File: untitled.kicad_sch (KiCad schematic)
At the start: 24 parts, among them J10_GPIO1 Conn_01x02, J11_SPI1 Conn_01x03, J2 Conn_01x04_Pin, J3 Conn_01x04_Pin, J4 Conn_01x02_Pin, J5 Conn_01x04_Pin, J6 Conn_01x04_Pin, J7 Conn_01x02_Pin, J9_GPIO1 Conn_01x02, J9_GPIO2 Conn_01x02

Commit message: Version 1.1 - reworked all smd's to 0603
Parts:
- R26, R31, R32, R33, R34: footprint Resistor_SMD:R_0201_0603Metric_Pad0.64x0.40mm_HandSolder -> Resistor_SMD:R_0603_1608Metric_Pad0.98x0.95mm_HandSolder
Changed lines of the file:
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@@
       (effects (font (size 1.27 1.27)) (justify left))
     )
-    (property "Footprint" "Resistor_SMD:R_0201_0603Metric_Pad0.64x0.40mm_HandSolder" (at 239.522 132.08 90)
+    (property "Footprint" "Resistor_SMD:R_0603_1608Metric_Pad0.98x0.95mm_HandSolder" (at 239.522 132.08 90)
       (effects (font (size 1.27 1.27)) hide)
     )
@@
       (effects (font (size 1.27 1.27)) (justify left))
     )
-    (property "Footprint" "Resistor_SMD:R_0201_0603Metric_Pad0.64x0.40mm_HandSolder" (at 210.312 69.85 90)
+    (property "Footprint" "Resistor_SMD:R_0603_1608Metric_Pad0.98x0.95mm_HandSolder" (at 210.312 69.85 90)
       (effects (font (size 1.27 1.27)) hide)
     )
@@
       (effects (font (size 1.27 1.27)) (justify left))
     )
-    (property "Footprint" "Resistor_SMD:R_0201_0603Metric_Pad0.64x0.40mm_HandSolder" (at 261.112 74.93 90)
+    (property "Footprint" "Resistor_SMD:R_0603_1608Metric_Pad0.98x0.95mm_HandSolder" (at 261.112 74.93 90)
       (effects (font (size 1.27 1.27)) hide)
     )
@@
       (effects (font (size 1.27 1.27)) (justify left))
     )
-    (property "Footprint" "Resistor_SMD:R_0201_0603Metric_Pad0.64x0.40mm_HandSolder" (at 256.032 74.93 90)
+    (property "Footprint" "Resistor_SMD:R_0603_1608Metric_Pad0.98x0.95mm_HandSolder" (at 256.032 74.93 90)
       (effects (font (size 1.27 1.27)) hide)
     )
@@
       (effects (font (size 1.27 1.27)) (justify left))
     )
-    (property "Footprint" "Resistor_SMD:R_0201_0603Metric_Pad0.64x0.40mm_HandSolder" (at 215.392 69.85 90)
+    (property "Footprint" "Resistor_SMD:R_0603_1608Metric_Pad0.98x0.95mm_HandSolder" (at 215.392 69.85 90)
       (effects (font (size 1.27 1.27)) hide)
     )
@@
       (effects (font (size 1.27 1.27)) (justify left))
     )
-    (property "Footprint" "Resistor_SMD:R_0201_0603Metric_Pad0.64x0.40mm_HandSolder" (at 259.842 132.08 90)
-      (effects (font (size 1.27 1.27)) hide)
-    )
+    (property "Footprint" "Resistor_SMD:R_0603_1608Metric_Pad0.98x0.95mm_HandSolder" (at 259.842 132.08 90)
+      (effects (font (size 1.27 1.27)) hide)
+    )

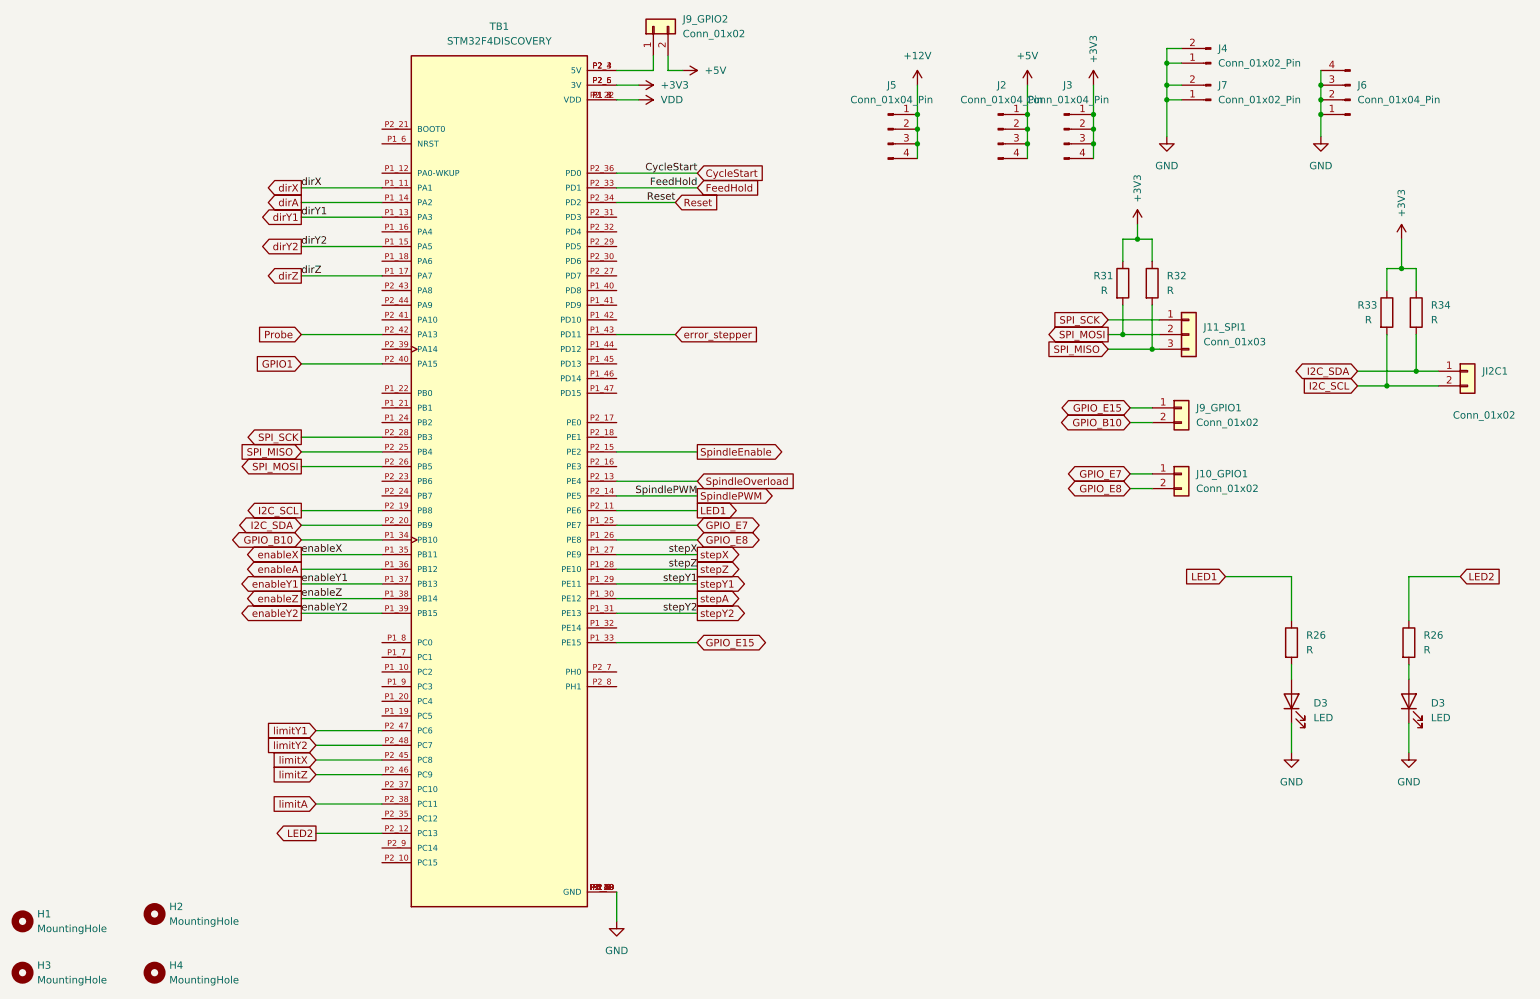
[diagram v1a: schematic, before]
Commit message: Adding Coolant and Mist; some GPIOs added
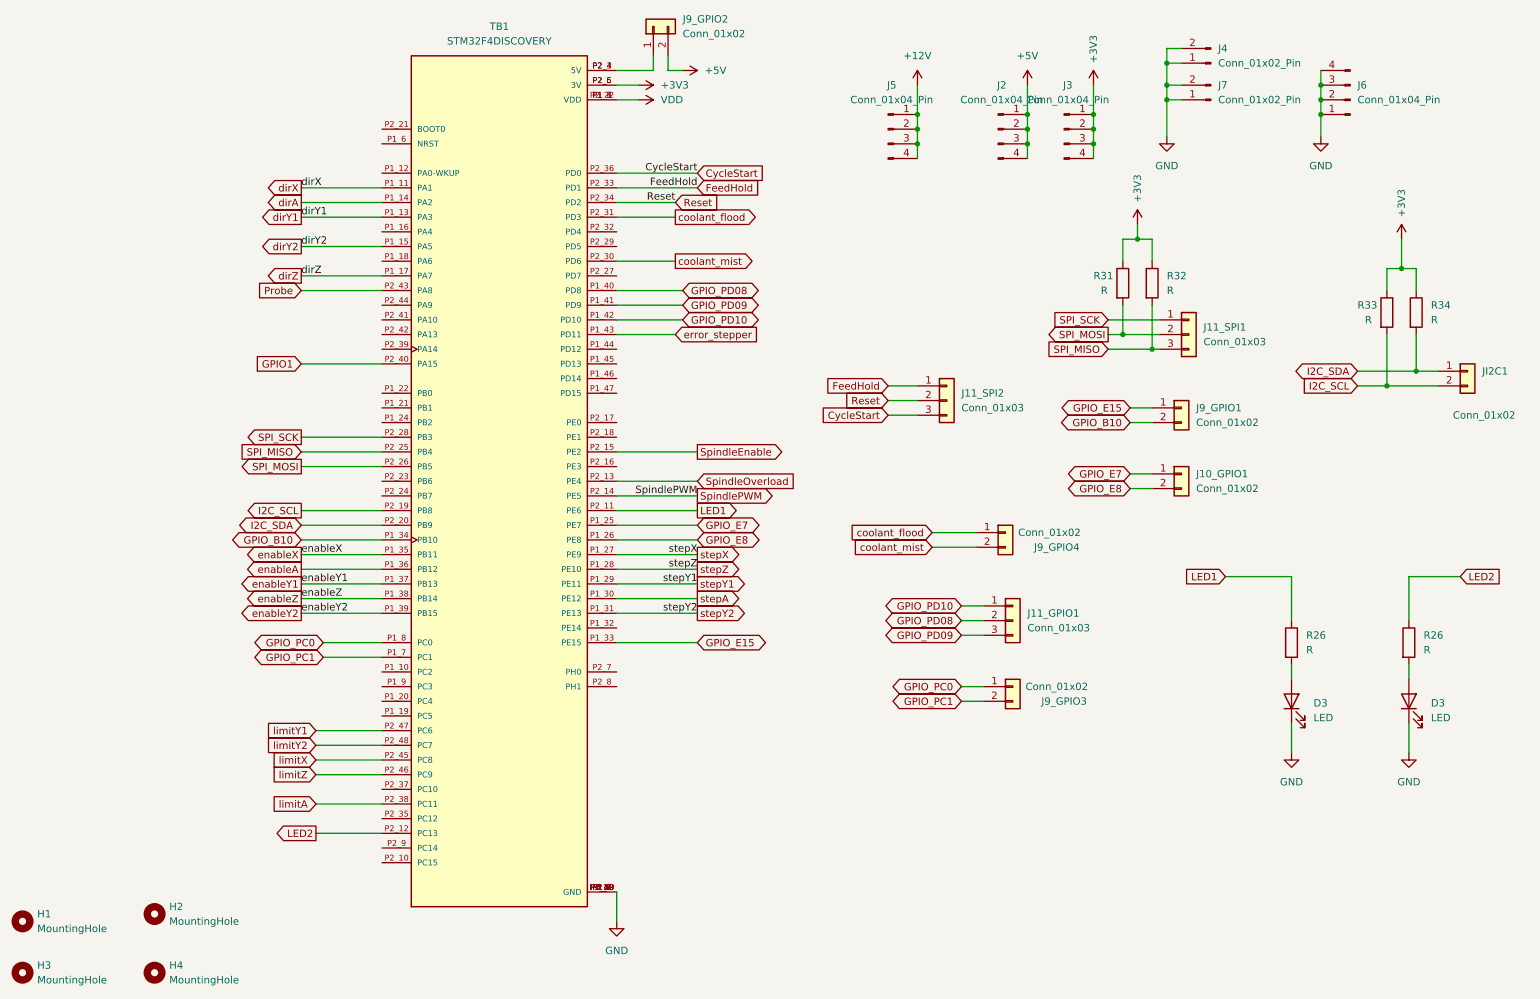
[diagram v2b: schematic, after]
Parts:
- added J11_GPIO1, J11_SPI2: Conn_01x03, Connector_PinHeader_2.54mm:PinHeader_1x03_P2.54mm_Vertical, symbol Connector_Generic:Conn_01x03
- added J9_GPIO3, J9_GPIO4: Conn_01x02, Connector_PinHeader_2.54mm:PinHeader_1x02_P2.54mm_Vertical, symbol Connector_Generic:Conn_01x02
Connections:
- net CycleStart: now also J11_SPI2.3 (Pin_3)
- net FeedHold: now also J11_SPI2.1 (Pin_1)
- net Probe: now also TB1.P2_43 (PA8); no longer TB1.P2_42 (PA13)
- net Reset: now also J11_SPI2.2 (Pin_2)
- net GPIO_PD08: now reaches TB1.P1_40 (PD8)
- net GPIO_PD08: now also J11_GPIO1.2 (Pin_2)
- net GPIO_PD09: now reaches TB1.P1_41 (PD9)
- net GPIO_PD09: now also J11_GPIO1.3 (Pin_3)
- net GPIO_PD10: now reaches TB1.P1_42 (PD10)
- net GPIO_PD10: now also J11_GPIO1.1 (Pin_1)
- net GPIO_PC1: now reaches TB1.P1_7 (PC1)
- net GPIO_PC1: now also J9_GPIO3.2 (Pin_2)
- net GPIO_PC0: now reaches TB1.P1_8 (PC0)
- net GPIO_PC0: now also J9_GPIO3.1 (Pin_1)
- net coolant_mist: now reaches TB1.P2_30 (PD6)
- net coolant_mist: now also J9_GPIO4.2 (Pin_2)
- net coolant_flood: now reaches TB1.P2_31 (PD3)
- net coolant_flood: now also J9_GPIO4.1 (Pin_1)

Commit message: Updating for version 1.1
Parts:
- R26: value R -> 510
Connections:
- net dirA: now also TB1.P1_17 (PA7); no longer TB1.P1_14 (PA2)
- net dirY2: now also TB1.P1_12 (PA0-WKUP); no longer TB1.P1_15 (PA5)
- net dirZ: now also TB1.P1_14 (PA2); no longer TB1.P1_17 (PA7)

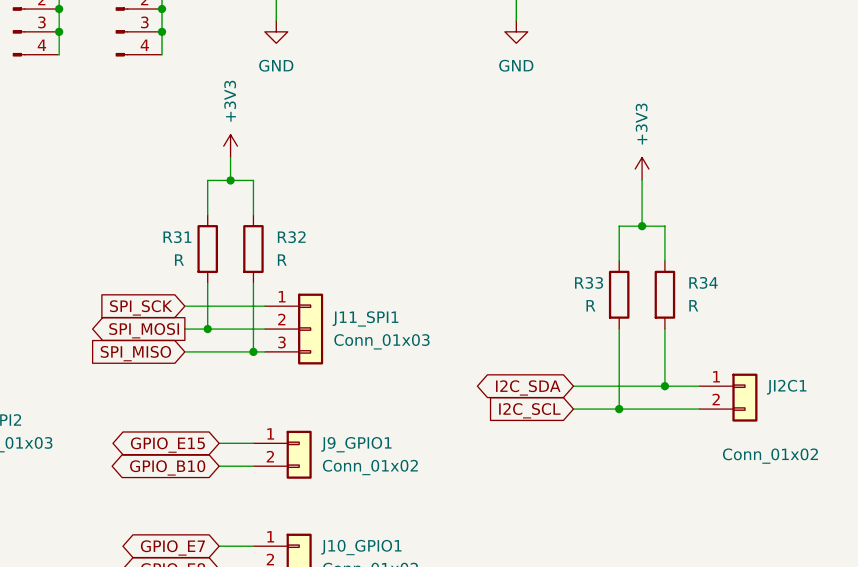
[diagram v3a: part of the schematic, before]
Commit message: Mainly value updates
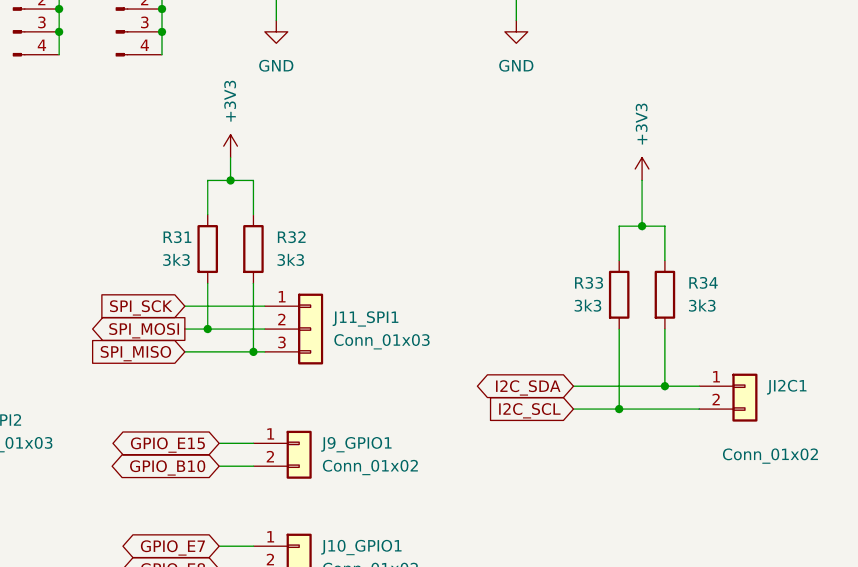
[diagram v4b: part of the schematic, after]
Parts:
- R31, R32, R33, R34: value R -> 3k3
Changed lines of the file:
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@@
       (effects (font (size 1.27 1.27)) (justify left))
     )
-    (property "Value" "R" (at 208.28 71.12 0)
+    (property "Value" "3k3" (at 207.01 71.12 0)
       (effects (font (size 1.27 1.27)) (justify left))
     )
@@
       (effects (font (size 1.27 1.27)) (justify left))
     )
-    (property "Value" "R" (at 265.43 76.2 0)
+    (property "Value" "3k3" (at 265.43 76.2 0)
       (effects (font (size 1.27 1.27)) (justify left))
     )
@@
       (effects (font (size 1.27 1.27)) (justify left))
     )
-    (property "Value" "R" (at 254 76.2 0)
+    (property "Value" "3k3" (at 252.73 76.2 0)
       (effects (font (size 1.27 1.27)) (justify left))
     )
@@
       (effects (font (size 1.27 1.27)) (justify left))
     )
-    (property "Value" "R" (at 219.71 71.12 0)
-      (effects (font (size 1.27 1.27)) (justify left))
-    )
+    (property "Value" "3k3" (at 219.71 71.12 0)
+      (effects (font (size 1.27 1.27)) (justify left))
+    )

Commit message: make mounting holes M3 friendly (3.2mm)
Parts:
- H1, H2, H3, H4: footprint MountingHole:MountingHole_2.5mm -> MountingHole:MountingHole_3.2mm_M3
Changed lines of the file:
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@@
       (effects (font (size 1.27 1.27)) (justify left))
     )
-    (property "Footprint" "MountingHole:MountingHole_2.5mm" (at 21.59 189.23 0)
+    (property "Footprint" "MountingHole:MountingHole_3.2mm_M3" (at 21.59 189.23 0)
       (effects (font (size 1.27 1.27)) hide)
     )
@@
       (effects (font (size 1.27 1.27)) (justify left))
     )
-    (property "Footprint" "MountingHole:MountingHole_2.5mm" (at 44.45 189.23 0)
+    (property "Footprint" "MountingHole:MountingHole_3.2mm_M3" (at 44.45 189.23 0)
       (effects (font (size 1.27 1.27)) hide)
     )
@@
       (effects (font (size 1.27 1.27)) (justify left))
     )
-    (property "Footprint" "MountingHole:MountingHole_2.5mm" (at 44.45 179.07 0)
+    (property "Footprint" "MountingHole:MountingHole_3.2mm_M3" (at 44.45 179.07 0)
       (effects (font (size 1.27 1.27)) hide)
     )
@@
       (effects (font (size 1.27 1.27)) (justify left))
     )
-    (property "Footprint" "MountingHole:MountingHole_2.5mm" (at 21.59 180.34 0)
-      (effects (font (size 1.27 1.27)) hide)
-    )
+    (property "Footprint" "MountingHole:MountingHole_3.2mm_M3" (at 21.59 180.34 0)
+      (effects (font (size 1.27 1.27)) hide)
+    )
